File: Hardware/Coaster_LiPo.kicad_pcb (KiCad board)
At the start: 2 copper layers, 90 x 90 mm, 17 parts, among them J1 USB_B_Mini, J2 Conn_02x03_Odd_Even, SW1 SW_SPDT, U1 MCP73831-2-OT, U2 ATtiny85-20SU

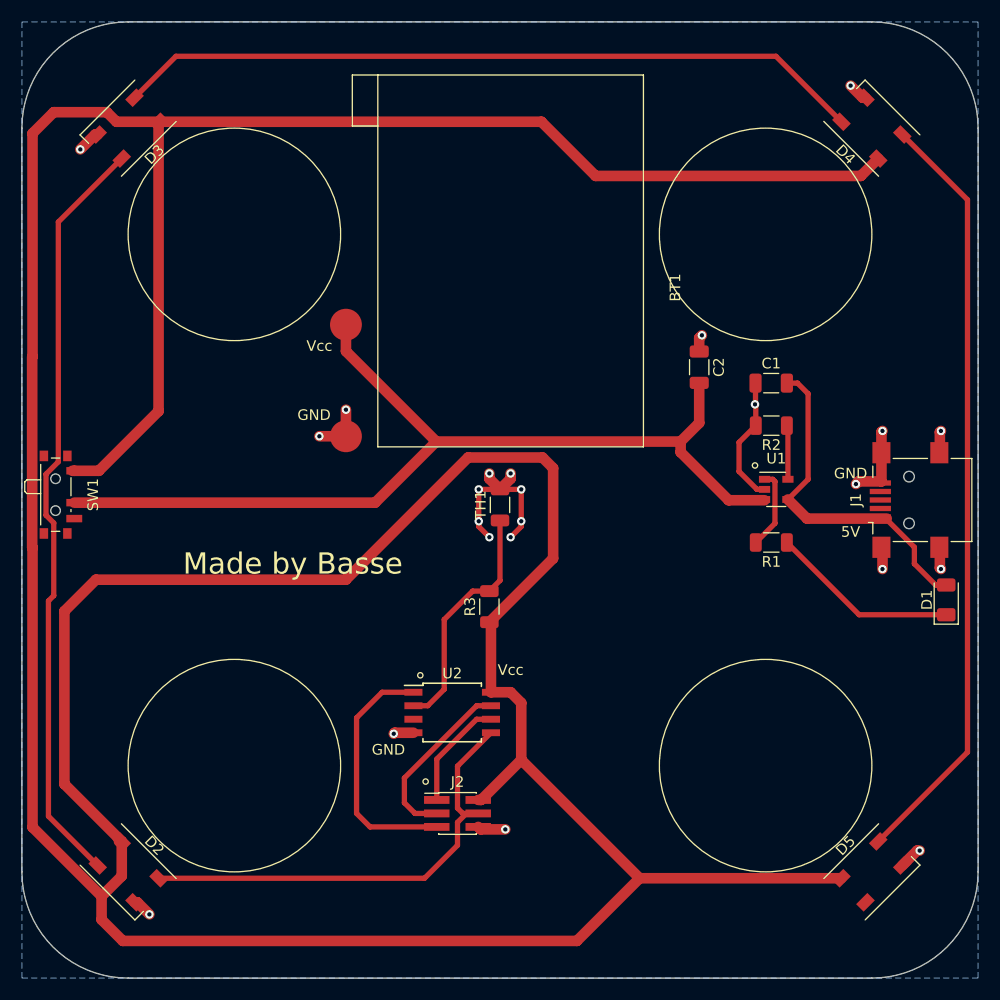
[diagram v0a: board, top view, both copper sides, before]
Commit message: Added graphics, rearranged components, added 4 more neopixels
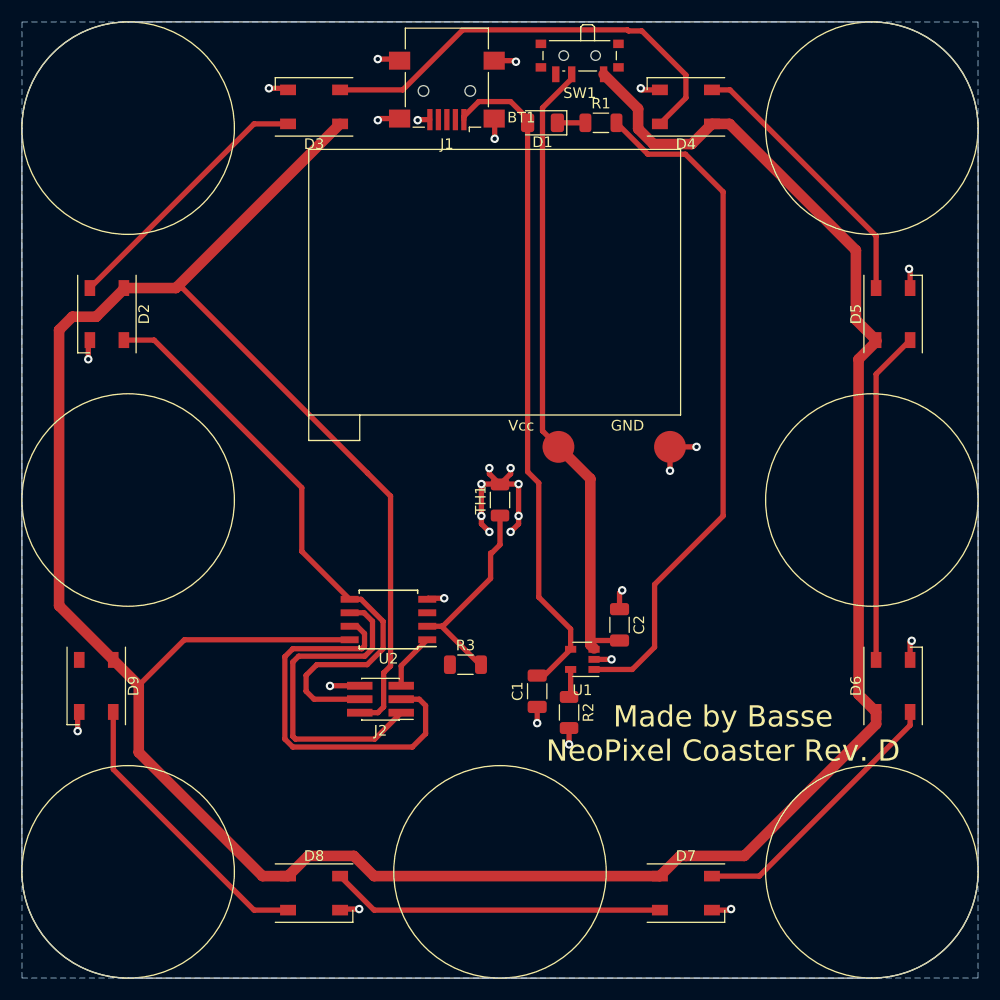
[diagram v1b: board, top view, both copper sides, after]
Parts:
- added D6: SK6812, LED_SMD:LED_SK6812_PLCC4_5.0x5.0mm_P3.2mm, F.Cu at (127.0, 112.5)
- added D7: SK6812, LED_SMD:LED_SK6812_PLCC4_5.0x5.0mm_P3.2mm, F.Cu at (107.5, 132.0)
- added D8: SK6812, LED_SMD:LED_SK6812_PLCC4_5.0x5.0mm_P3.2mm, F.Cu at (72.5, 132.0)
- added D9: SK6812, LED_SMD:LED_SK6812_PLCC4_5.0x5.0mm_P3.2mm, F.Cu at (52.0, 112.5)
- added G***: LOGO, MyOwn:Flower_logo, B.Cu at (89.5, 95.0)
- D1: footprint Diode_SMD:D_1206_3216Metric -> LED_SMD:LED_1206_3216Metric
- R1: value 1k -> 2.2k
- moved SW1 63.9 mm to (97.5, 53.5), turned to 180 degrees
- moved D1 58.8 mm to (94.0, 59.5), turned to 180 degrees
- moved J1 58.1 mm to (85.0, 56.5), turned to 180 degrees
- moved D2 52.5 mm to (53.0, 77.5), turned to 270 degrees
- moved D5 52.5 mm to (127.0, 77.5), turned to 90 degrees
- moved R1 42.6 mm to (99.5, 59.5), turned to 0 degrees
- moved C1 36.4 mm to (93.5, 113.0), turned to 90 degrees
- moved R2 33.0 mm to (96.5, 115.0), turned to 270 degrees
- moved C2 25.4 mm to (101.2, 106.8)
- moved U1 24.3 mm to (97.8, 110.0), turned to 180 degrees
- moved D3 17.6 mm to (72.5, 58.0), turned to 180 degrees
- moved D4 17.6 mm to (107.5, 58.0), turned to 180 degrees
- moved J2 13.0 mm to (78.8, 113.8), turned to 180 degrees
- moved U2 10.6 mm to (79.5, 106.2), turned to 180 degrees
- moved R3 5.91 mm to (86.8, 110.5), turned to 0 degrees
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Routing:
- net Vcc: track 407.1 -> 311.7 mm
- net Net-(R1-Pad2): track 7.55 -> 64.8 mm
- net Net-(D2-Pad4): track 71.9 -> 25.0 mm
- net Net-(D4-Pad4): track 72.6 -> 26.0 mm
- net Net-(D7-Pad4): track 0.00 -> 31.4 mm
- net Net-(D5-Pad4): track 0.00 -> 31.4 mm
- net Net-(BT1-Pad1): track 91.0 -> 60.1 mm
- net Net-(C1-Pad2): track 32.9 -> 63.3 mm
- net Net-(D3-Pad4): track 70.7 -> 42.3 mm
- net Net-(D8-Pad4): track 0.00 -> 27.3 mm
- net Net-(D6-Pad4): track 0.00 -> 25.8 mm
- net SCK: track 16.8 -> 37.8 mm
- net MISO: track 10.5 -> 31.4 mm
- net Reset: track 23.4 -> 5.34 mm
- net Net-(D1-Pad1): track 17.8 -> 2.64 mm
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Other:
- board text added: "Made by Basse NeoPixel Coaster Rev. D"
- board text removed: "5V"
- board text removed: "Made by Basse"
- board text removed: "NeoPixel Coaster"

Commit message: Added push button to cycle through LED modes
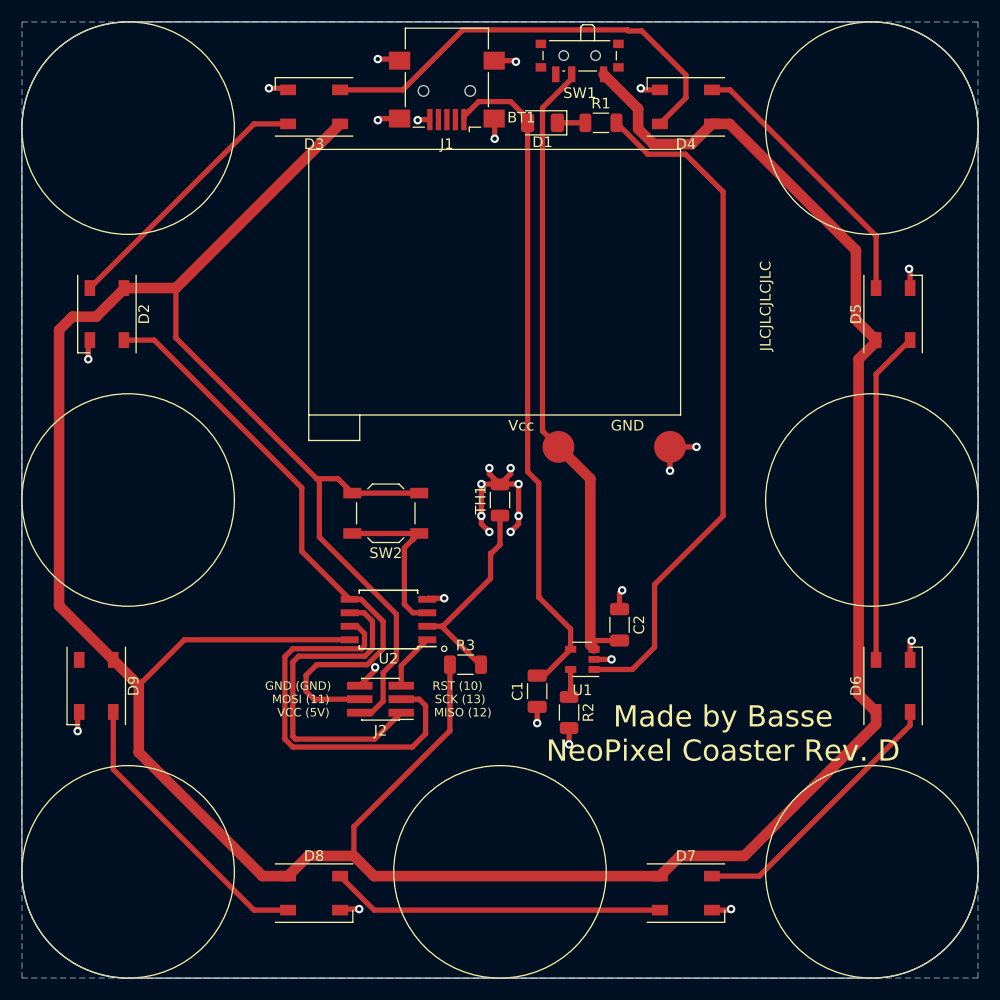
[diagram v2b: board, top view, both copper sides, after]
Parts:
- removed the G*** at (89.5, 95.0)
- added G***: LOGO, MyOwn:Flower_logo4, B.Cu at (90.0, 95.0)
- added REF**: Distans, MyOwn:Distans, F.Cu at (55.0, 95.0)
- added REF**: Distans, MyOwn:Distans, F.Cu at (125.0, 95.0)
- added REF**: Distans, MyOwn:Distans, F.Cu at (90.0, 130.0)
- added REF**: Distans, MyOwn:Distans, F.Cu at (125.0, 130.0)
- added REF**: Distans, MyOwn:Distans, F.Cu at (55.0, 130.0)
- added REF**: Distans, MyOwn:Distans, F.Cu at (125.0, 60.0)
- added REF**: Distans, MyOwn:Distans, F.Cu at (55.0, 60.0)
- added SW2: SW_Push, Button_Switch_SMD:SW_SPST_TL3342, F.Cu at (79.2, 96.2)
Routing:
- net Vcc: track 311.7 -> 343.4 mm
- net Net-(SW2-Pad1): track 0.00 -> 16.1 mm
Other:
- board text added: "GND (GND)"
- board text added: "JLCJLCJLCJLC"
- board text added: "MISO (12)"
- board text added: "MOSI (11)"
- board text added: "RST (10)"
- board text added: "SCK (13)"
- board text added: "VCC (5V)"

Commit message: Moved a via and limited logo
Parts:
- G***: moved to F.Cu
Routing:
- net GND: track 56.6 -> 58.2 mm
